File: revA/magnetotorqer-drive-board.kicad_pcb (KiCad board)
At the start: 2 copper layers, 90.2 x 101.1 mm, 281 parts, among them J1 ZX62-AB-5PA(31), J2 T1M-02-F-SH-L, J3 T1M-02-F-SH-L, J4 T1M-02-F-SH-L, J5 T1M-02-F-SH-L, J6 T1M-02-F-SH-L, J7 T1M-02-F-SH-L, J8 Conn_01x06, J9 Conn_02x02_Top_Bottom, P2 FTSH-105-01-F-DV-K-TR, Q1 MMDT2222A, Q3 MMDT2222A, Q4 IRLML2803, Q5 MMBT4401WT1G, Q6 MMDT2222A, Q7 BSZ180, Q8 BSZ180, Q9 MMDT2222A, SW1 KMR231NG LFS, U1 74LVC1G17, U10 INA199A2xDCK, U11 DAC121S101Q, U12 AD5270BRM, U13 LTC3600, U14 DAC121S101Q, U15 AD5270BRM, U16 LTC3600, U17 INA199A2xDCK, U18 DRV8838DSGT, U19 DRV8838DSGT, U2 74LVC1G17, U20 AP2161W, U21 MCP1700T-33, U22 MCP1700T-50, U23 MCP1700T-33, U24 ATL431BQ, U25 DAC121S101Q, U26 AD5270BRM, U27 LTC3600, U3 MCP9700AT-E/LT, U4 MCP9700AT-E/LT, U5 DRV8838DSGT, U6 MR25H10MDF, U7 MAX708RESA-T, U8 ATSAMD51J20A-A, U9 INA199A2xDCK, Y1 32.768kHz

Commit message: working
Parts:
- added P1: Card Edge for HSEC8-160-01-S-DV-A-K-TR, SierraLobo:HSEC8-160-CARD-EDGE, F.Cu at (109.0, 53.4)
- added Q2: MMBT3906T, Package_TO_SOT_SMD:SOT-523, F.Cu at (72.1, 42.4)
- added R102: 0, Resistor_SMD:R_0603_1608Metric, F.Cu at (204.5, 77.0)
- added R103: 0, Resistor_SMD:R_0603_1608Metric, F.Cu at (247.4, 52.1)
- added R104: 0, Resistor_SMD:R_0603_1608Metric, F.Cu at (204.5, 81.5)
- C48, C52, R59: moved to B.Cu
- moved LED3 174.2 mm to (72.7, 48.9)
- moved LED4 174.2 mm to (74.9, 48.9)
- moved Q9 172.2 mm to (76.5, 37.7)
- moved R85 169.6 mm to (75.8, 40.6)
- moved R87 169.6 mm to (75.8, 42.6)
- moved R28 161.9 mm to (64.5, 40.2)
- moved R32 161.9 mm to (64.5, 42.2)
- moved R86 161.8 mm to (72.4, 37.0)
- moved R88 161.8 mm to (72.4, 39.5)
- moved Q1 154.6 mm to (65.2, 37.3)
- moved LED1 143.1 mm to (77.2, 48.9)
- moved LED2 143.1 mm to (79.5, 48.9)
- moved R31 140.5 mm to (61.1, 41.6)
- moved R26 138.5 mm to (61.1, 36.6)
- moved R27 138.5 mm to (61.1, 39.1)
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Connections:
- TP18 pad 1: /X Driver/Adjustable Buck Regulator 1/VSET -> Net-(R103-Pad2)
- TP29 pad 1: /Z Driver/Adjustable Buck Regulator 1/VSET -> Net-(R104-Pad2)
- TP9 pad 1: /Y Driver/Adjustable Buck Regulator 1/VSET -> Net-(R102-Pad2)

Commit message: placement
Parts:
- removed TP17, TP4, TP8: ${NET_NAME(1)}, TestPoint:TestPoint_Keystone_5000-5004_Miniature
- C11, C12, C17, C18, C19, C20, C21, C22, C23, C24, C27, C28, C30, C31, C33, C34, C35, C36, C37, C38, C42, C44, C45, C46, C47, C5, C54, C56, C57, C58, C59, C6, C60, C61, C63, C64, C67, C68, C69, C70, C71, C72, C73, C74, C75, C76, C77, C78, C79, C83, LED1, LED2, LED4, Q3, Q6, R101, R15, R23, R33, R34, R35, R43, R45, R47, R48, R49, R57, R68, R70, R74, R75, R76, R77, R80, R81, R82, R89, R90, R91, R99, U20: moved to B.Cu
- R46, R8, R9: footprint Resistor_SMD:R_0603_1608Metric -> Resistor_SMD:R_0805_2012Metric
- moved TP3 152.4 mm to (133.1, 109.2)
- moved TP1 144.6 mm to (142.0, 102.6), turned to 90 degrees
- moved C44 143.4 mm to (113.5, 96.8), turned to -90 degrees
- moved TP2 142.2 mm to (142.0, 98.8), turned to 90 degrees
- moved TP19 141.0 mm to (114.8, 109.2)
- moved C52 140.8 mm to (127.0, 102.6)
- moved U16 140.6 mm to (122.4, 101.6)
- moved L3 139.9 mm to (130.8, 101.6)
- moved C49 139.9 mm to (125.0, 105.7)
- moved C53 139.9 mm to (125.0, 97.5)
- moved R59 139.8 mm to (127.0, 99.3), turned to -90 degrees
- moved C48 139.3 mm to (112.3, 102.1)
- moved C51 139.0 mm to (120.4, 105.7), turned to 0 degrees
- moved C45 138.9 mm to (115.6, 96.8)
- moved TP22 138.8 mm to (122.2, 109.2)
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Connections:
- C11 pad 1: +3V3 -> +3V3D
- C12 pad 1: +3V3 -> +3V3D
- C19 pad 1: +3V3 -> +3V3D
- C20 pad 1: +3V3 -> +3V3D
- C21 pad 1: +3V3 -> +3V3A
- C22 pad 1: +3V3 -> +3V3D
- C23 pad 1: +3V3 -> +3V3A
- C24 pad 1: +3V3 -> +3V3D
- C25 pad 1: +3V3 -> +3V3D
- C26 pad 1: +3V3 -> +3V3D
- C28 pad 1: /X Driver/Current Feedback 1/VCC -> +3V3A
- C29 pad 1: +3V3 -> +1V65A
- C30 pad 1: /X Driver/Current Feedback 1/VCC -> +3V3A
- C31 pad 1: /Y Driver/Current Feedback 1/VCC -> +3V3A
- C32 pad 1: +3V3 -> +1V65A
- C33 pad 1: /Y Driver/Current Feedback 1/VCC -> +3V3A
- C5 pad 1: +3V3 -> +3V3D
- C54 pad 1: /Z Driver/Current Feedback 1/VCC -> +3V3A
- C55 pad 1: +3V3 -> +1V65A
- C56 pad 1: /Z Driver/Current Feedback 1/VCC -> +3V3A
- C57 pad 1: +3V3 -> +3V3D
- C58 pad 1: +3V3 -> +3V3D
- C6 pad 1: +3V3 -> +3V3D
- C71 pad 1: +3V3 -> +3V3D
- C73 pad 1: +3V3 -> +3V3A
- C74 pad 1: +3V3 -> +1V65A
- J9 pad 2: Net-(J9-Pin_1) -> +5VA
- J9 pad 3: VAA -> Net-(J9-Pin_1)
- J9 pad 4: +5VA -> VAA
- P2 pad 1: +3V3 -> +3V3D
- R15 pad 2: +3V3 -> +3V3D
- R17 pad 1: +3V3 -> +3V3D
- R2 pad 1: /TX_MCU -> /TX
- R20 pad 1: +3V3 -> +3V3D
- R3 pad 1: +3V3 -> +3V3A
- R39 pad 2: +3V3 -> +3V3D
- R4 pad 1: +3V3 -> +3V3A
- R46 pad 1: /Z Driver/OUT2_SEN -> /Z Driver/OUT1_SEN
- R46 pad 2: /Z- -> /Z+
- R5 pad 1: +3V3 -> +3V3A
- R53 pad 2: +3V3 -> +3V3D
- R6 pad 1: +3V3 -> +3V3A
- R7 pad 1: +3V3 -> +3V3A
- R8 pad 1: /X Driver/OUT2_SEN -> /X Driver/OUT1_SEN
- R8 pad 2: /X- -> /X+
- R82 pad 2: +3V3 -> +1V65A
- R83 pad 1: +3V3 -> +1V65A
- R87 pad 1: +3V3 -> +3V3D
- R9 pad 1: /Y Driver/OUT2_SEN -> /Y Driver/OUT1_SEN
- R9 pad 2: /Y- -> /Y+
- R95 pad 2: +3V3 -> +3V3D
- TP24 pad 1: +3V3 -> +3V3D
- TP26 pad 1: +3V3 -> +3V3A
- TP27 pad 1: +3V3 -> +1V65A
- U1 pad 4: /RX_MCU -> /RX
- U1 pad 5: +3V3 -> +3V3D
- U10 pad 1: +3V3 -> +1V65A
- U10 pad 3: /Y Driver/Current Feedback 1/VCC -> +3V3A
- U10 pad 4: /Y- -> /Y+
- U10 pad 5: /Y Driver/OUT2_SEN -> /Y Driver/OUT1_SEN
- U17 pad 1: +3V3 -> +1V65A
- U17 pad 3: /Z Driver/Current Feedback 1/VCC -> +3V3A
- U17 pad 4: /Z- -> /Z+
- U17 pad 5: /Z Driver/OUT2_SEN -> /Z Driver/OUT1_SEN
- U18 pad 2: /X+ -> /X Driver/OUT1_SEN
- U18 pad 3: /X Driver/OUT2_SEN -> /X-
- U18 pad 8: +3V3 -> +3V3D
- U19 pad 2: /Z+ -> /Z Driver/OUT1_SEN
- U19 pad 3: /Z Driver/OUT2_SEN -> /Z-
- U19 pad 8: +3V3 -> +3V3D
- U2 pad 5: +3V3 -> +3V3D
- U21 pad 3: +3V3 -> +3V3D
- U23 pad 3: +3V3 -> +3V3A
- U24 pad 2: +3V3 -> +1V65A
- U5 pad 2: /Y+ -> /Y Driver/OUT1_SEN
- U5 pad 3: /Y Driver/OUT2_SEN -> /Y-
- U5 pad 8: +3V3 -> +3V3D
- U6 pad 8: +3V3 -> +3V3D
- U7 pad 2: +3V3 -> +3V3D
- U8 pad 21: +3V3 -> +3V3D
- U8 pad 34: +3V3 -> +3V3D
- U8 pad 48: +3V3 -> +3V3D
- U8 pad 56: +3V3 -> +3V3D
- U8 pad 8: +3V3 -> +3V3A
- U9 pad 1: +3V3 -> +1V65A
- U9 pad 3: /X Driver/Current Feedback 1/VCC -> +3V3A
- U9 pad 4: /X- -> /X+
- U9 pad 5: /X Driver/OUT2_SEN -> /X Driver/OUT1_SEN

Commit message: Update magnetotorqer-drive-board.kicad_pcb
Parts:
- moved LED3 3.30 mm to (73.2, 52.3), turned to -90 degrees
- moved LED1 0.89 mm to (75.6, 52.3), turned to -90 degrees
- moved LED2 0.63 mm to (71.8, 52.3), turned to -90 degrees
- moved LED4 0.25 mm to (78.7, 52.3), turned to -90 degrees

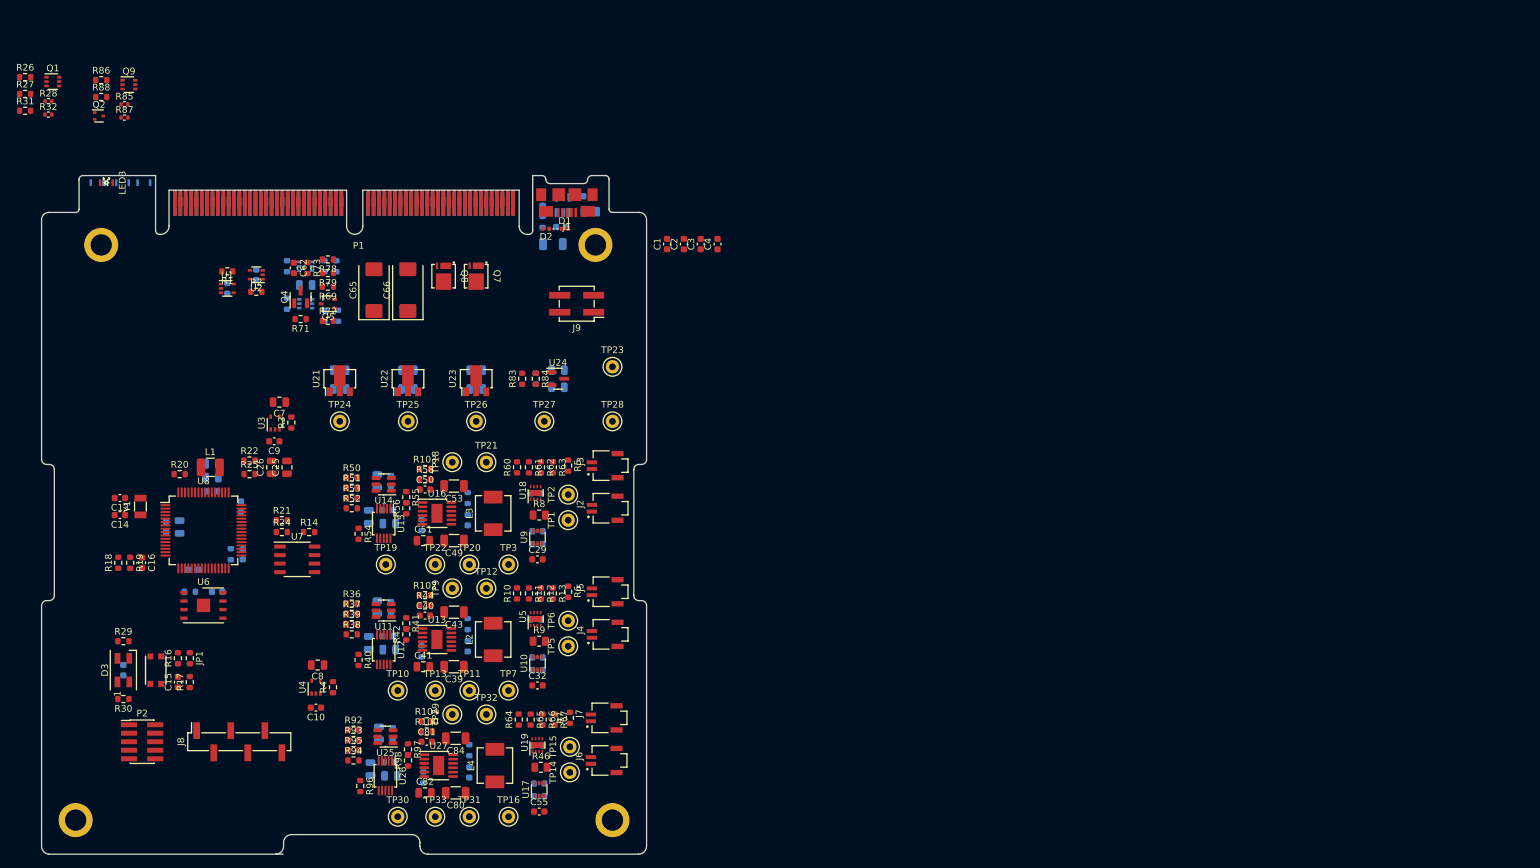
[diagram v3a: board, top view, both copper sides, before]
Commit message: routing mostly complete
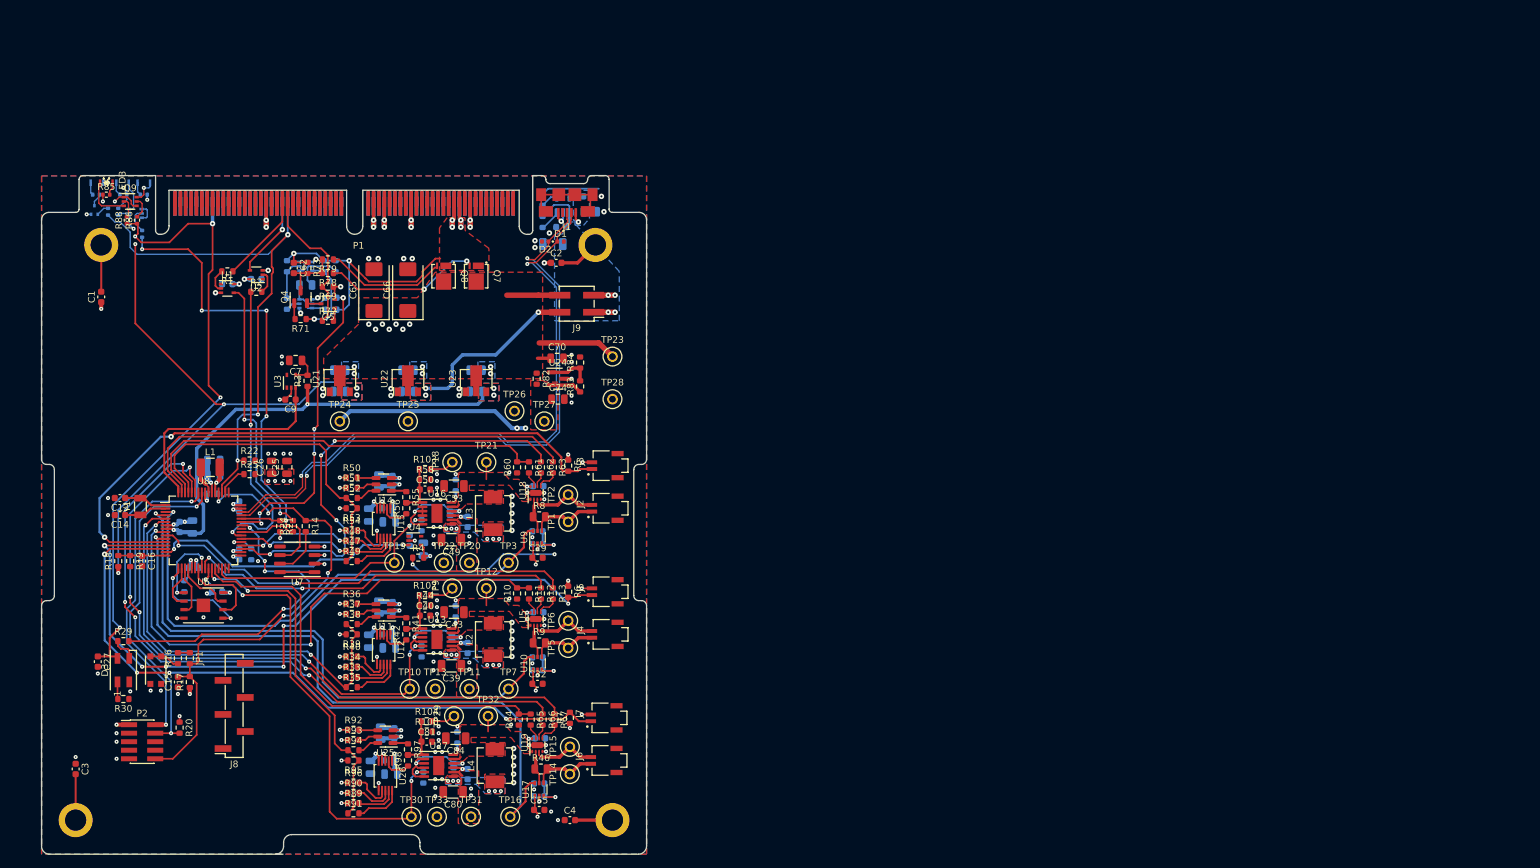
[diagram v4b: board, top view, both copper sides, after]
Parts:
- C10, C41, C51, C8, C82, Q1, Q2, R28, R32, R87: moved to B.Cu
- C27, C70, C74, R33, R34, R35, R47, R48, R49, R82, R89, R90, R91: moved to F.Cu
- R26, R27, R31: footprint Resistor_SMD:R_0603_1608Metric -> Resistor_SMD:R_0402_1005Metric; moved to B.Cu
- R86, R88: footprint Resistor_SMD:R_0603_1608Metric -> Resistor_SMD:R_0402_1005Metric
- TP1, TP10, TP11, TP12, TP13, TP14, TP15, TP16, TP18, TP19, TP2, TP20, TP21, TP22, TP23, TP24, TP25, TP26, TP27, TP28, TP29, TP3, TP30, TP31, TP32, TP33, TP5, TP6, TP7, TP9: footprint TestPoint:TestPoint_Keystone_5000-5004_Miniature -> SierraLobo:TestPoint_Keystone_5000-5004_Miniature
- moved C3 121.6 mm to (68.6, 139.7), turned to -90 degrees
- moved C4 88.6 mm to (142.2, 147.3), turned to 0 degrees
- moved C1 84.7 mm to (72.4, 69.3)
- moved R20 37.8 mm to (84.1, 133.5), turned to -90 degrees
- moved R26 29.1 mm to (78.5, 59.9), turned to -90 degrees
- moved C10 28.5 mm to (118.4, 105.7), turned to 90 degrees
- moved U4 26.3 mm to (119.1, 105.7), turned to 0 degrees
- moved C8 23.4 mm to (120.4, 106.9), turned to 90 degrees
- moved Q1 23.2 mm to (77.5, 56.9), turned to 180 degrees
- moved R4 23.1 mm to (119.6, 108.2), turned to 0 degrees
- moved R27 22.4 mm to (74.9, 56.6), turned to 90 degrees
- moved R86 21.5 mm to (77.7, 57.9), turned to 90 degrees
- moved R31 19.5 mm to (73.4, 56.6), turned to -90 degrees
- moved C2 19.2 mm to (140.2, 64.3), turned to 0 degrees
- moved R88 18.8 mm to (76.2, 57.9), turned to 90 degrees
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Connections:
- J1 pad 6: GND -> unconnected-(J1-Shield-Pad6)
- Q2 pad 2: LED_PWR -> LED_VCC
- R27 pad 2: LED_PWR -> LED_VCC
- R28 pad 1: LED_PWR -> LED_VCC
- R40 pad 1: +5VA -> +3V3D
- R54 pad 1: +5VA -> +3V3D
- R86 pad 1: LED_PWR -> LED_VCC
- R88 pad 1: LED_PWR -> LED_VCC
- R96 pad 1: +5VA -> +3V3D
- U8 pad 15: /Control/AIN6 -> /TEMP_B
- U8 pad 35: /Control/PA16 -> /X_PH_EN
- U8 pad 64: /X_PH_EN -> /TEMP_A
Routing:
- net GND: track 0.00 -> 125.4 mm, vias 0 -> 151
- net VAA: track 0.00 -> 118.6 mm, vias 0 -> 23
- net LED_VCC: track 0.00 -> 115.4 mm, vias 0 -> 6
- net +3V3A: track 0.00 -> 109.8 mm, vias 0 -> 12
- net /Y_TEMP: track 0.00 -> 108.0 mm, vias 0 -> 6
- net /Z_HB_PH: track 0.00 -> 101.8 mm, vias 0 -> 4
- net /Z_PH_EN: track 0.00 -> 101.8 mm, vias 0 -> 4
- net /Z_VRSEN: track 0.00 -> 100.6 mm, vias 0 -> 1
- net /Z_TEMP: track 0.00 -> 100.5 mm, vias 0 -> 4
- net /X_TEMP: track 0.00 -> 96.4 mm, vias 0 -> 2
- net /D+: track 0.00 -> 93.6 mm, vias 0 -> 2
- net /D-: track 0.00 -> 92.9 mm, vias 0 -> 2
- net /Y_VRSEN: track 0.00 -> 85.4 mm, vias 0 -> 1
- net /~{Y_HB_SLEEP}: track 0.00 -> 81.2 mm, vias 0 -> 2
- net /~{FAULT}: track 0.00 -> 81.0 mm, vias 0 -> 3
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- added copper zone on F.Cu, net +1V65A
- added copper zone on In2.Cu, net +1V65A
- added copper zone on B.Cu, net +3V3A
- added copper zone on F.Cu, net +3V3A
- added copper zone on In2.Cu, net +3V3A
- added copper zone on B.Cu, net +3V3D
- added copper zone on F.Cu, net +3V3D
- added copper zone on In2.Cu, net +3V3D
- added copper zone on B.Cu, net +5VA
- added copper zone on F.Cu, net +5VA
- added copper zone on In2.Cu, net +5VA
- added copper zone on B.Cu, net /5V_USB
- added copper zone on F.Cu, net /VBATT
- added copper zone on B.Cu, net /X Driver/Adjustable Buck Regulator 1/SW
- added copper zone on F.Cu, net /X Driver/Adjustable Buck Regulator 1/SW
- added copper zone on F.Cu, net /X Driver/VDRV
- added copper zone on B.Cu, net /Y Driver/Adjustable Buck Regulator 1/SW
- added copper zone on F.Cu, net /Y Driver/Adjustable Buck Regulator 1/SW
- added copper zone on F.Cu, net /Y Driver/VDRV
- added copper zone on B.Cu, net /Z Driver/Adjustable Buck Regulator 1/SW
- added copper zone on F.Cu, net /Z Driver/Adjustable Buck Regulator 1/SW
- added copper zone on F.Cu, net /Z Driver/VDRV
- added copper zone on B.Cu, net GND
- added copper zone on F.Cu, net GND
- added copper zone on In1.Cu, net GND
- added copper zone on B.Cu, net Net-(J9-Pin_1)
- added copper zone on B.Cu, net VAA
- added copper zone on F.Cu, net VAA
- added copper zone on In2.Cu, net VAA
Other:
- copper layers 2 -> 4
